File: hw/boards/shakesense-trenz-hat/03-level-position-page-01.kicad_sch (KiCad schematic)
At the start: 11 parts, among them J2 Passive GNSS antenna, U20 SCL3300-D01, U21 MAX-M10S

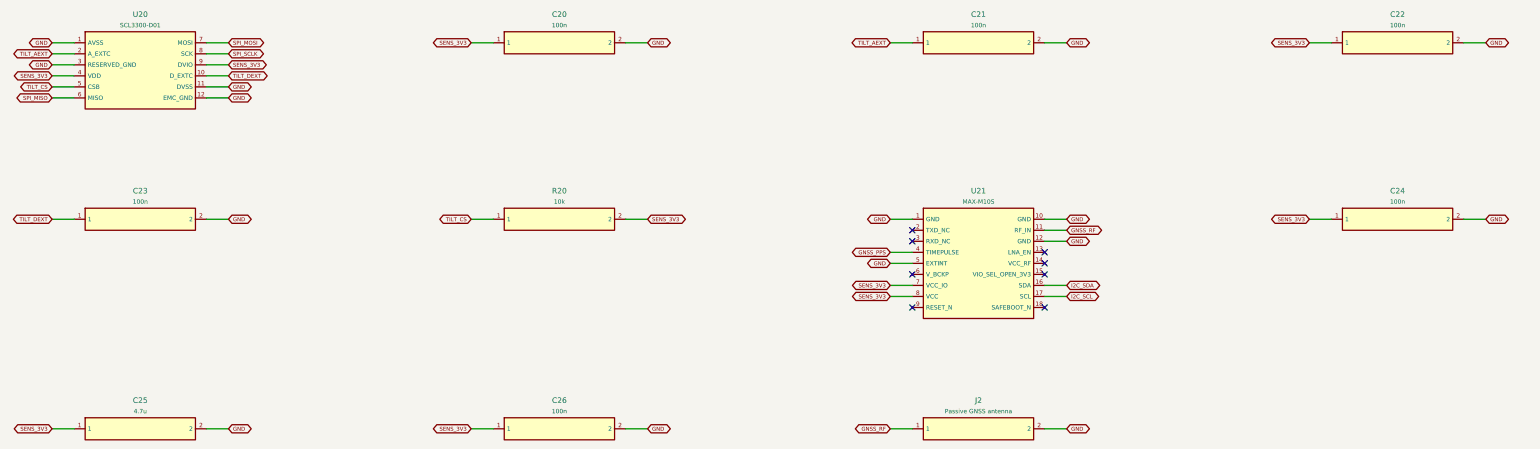
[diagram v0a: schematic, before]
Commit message: Expose Trenz GPIOs on the Pi-outline HDI sensor HAT
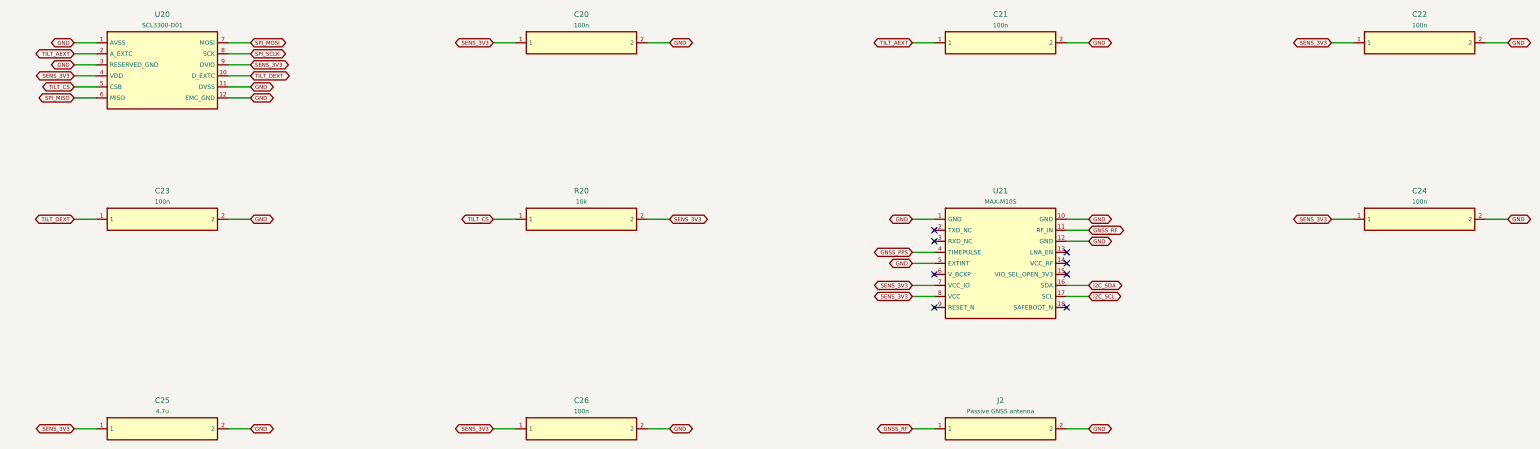
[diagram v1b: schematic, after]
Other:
- title: shakesense-trenz-hat / 03-level-position-page-01 -> ShakeSense T1 / 03-level-position-page-01
- moved on the sheet: C20, C21, C22, C23, C24, C25, C26, J2, R20, U20, U21

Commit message: Replace T1 GNSS with single Racotech geophone input
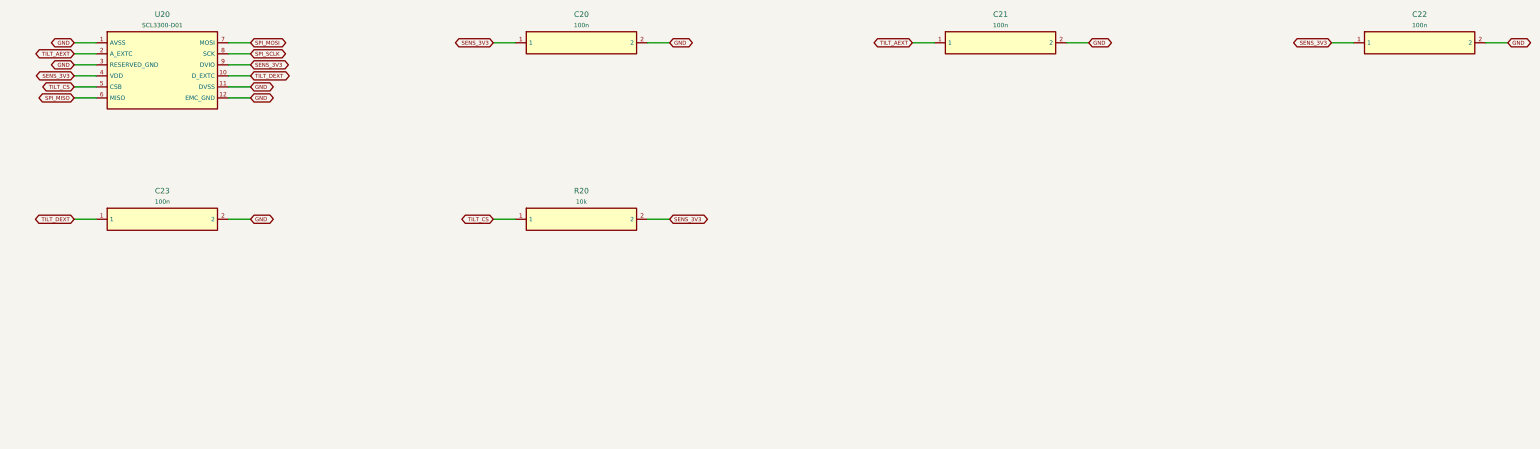
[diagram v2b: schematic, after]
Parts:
- removed C24: 100n, ShakeSense:Capacitor_SMD__C_0603_1608Metric, symbol ShakeSense:Part_C24
- removed C25: 4.7u, ShakeSense:Capacitor_SMD__C_0805_2012Metric, symbol ShakeSense:Part_C25
- removed C26: 100n, ShakeSense:Capacitor_SMD__C_0603_1608Metric, symbol ShakeSense:Part_C26
- removed J2: Passive GNSS antenna, ShakeSense:Connector_Coaxial__U.FL_Hirose_U.FL-R-SMT-1_Vertical, symbol ShakeSense:Part_J2
- removed U21: MAX-M10S, ShakeSense:RF_GPS__ublox_MAX, symbol ShakeSense:Part_U21
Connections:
- no-connect marks 8 -> 0
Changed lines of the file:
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@@
-(kicad_sch (version 20230121) (generator eeschema) (paper "A3") (title_block (title "ShakeSense T1 / 03-level-position-page-01") (date "2026-09-24") (rev "T1-GPIO"))
+(kicad_sch (version 20230121) (generator eeschema) (paper "A3") (title_block (title "ShakeSense T1 / 03-level-position-page-01") (date "2026-09-24") (rev "T1-GEO"))
 (symbol (lib_id "ShakeSense:Part_U20") (at 50.8 44.45 0) (unit 1) (in_bom yes) (on_board yes) (dnp no)
               (property "Reference" "U20" (at 50.8 31.560000000000002 0) (effects (font (size 1.27 1.27))))
@@
 (wire (pts (xy 162.56 78.74) (xy 167.64 78.74)) (stroke (width 0) (type default)))
 (global_label "SENS_3V3" (shape bidirectional) (at 167.64 78.74 0) (effects (font (size 0.9 0.9)) (justify left)))
-(symbol (lib_id "ShakeSense:Part_U21") (at 243.83999999999997 88.9 0) (unit 1) (in_bom yes) (on_board yes) (dnp no)
-              (property "Reference" "U21" (at 243.83999999999997 72.2 0) (effects (font (size 1.27 1.27))))
-              (property "Value" "MAX-M10S" (at 243.83999999999997 74.7 0) (effects (font (size 1.0 1.0))))
-              (property "Footprint" "ShakeSense:RF_GPS__ublox_MAX" (at 243.83999999999997 88.9 0) (effects (font (size 1 1)) hide))
-              (property "MPN" "MAX-M10S-00B" (at 243.83999999999997 88.9 0) (effects (font (size 1 1)) hide))
-              (instances (project "shakesense-trenz-hat" (path "/4ffaaa5d-c728-540d-9f0f-f1cafbdbe36e/30b3f632-5bdc-5bfd-9387-e670932c7991" (reference "U21") (unit 1)))))
-(wire (pts (xy 228.6 78.74) (xy 223.52 78.74)) (stroke (width 0) (type default)))
-(global_label "GND" (shape bidirectional) (at 223.52 78.74 180) (effects (font (size 0.9 0.9)) (justify right)))
-(no_connect (at 228.6 81.28))
-(no_connect (at 228.6 83.82))
-(wire (pts (xy 228.6 86.36) (xy 223.52 86.36)) (stroke (width 0) (type default)))
-(global_label "GNSS_PPS" (shape bidirectional) (at 223.52 86.36 180) (effects (font (size 0.9 0.9)) (justify right)))
-(wire (pts (xy 228.6 88.9) (xy 223.52 88.9)) (stroke (width 0) (type default)))
-(global_label "GND" (shape bidirectional) (at 223.52 88.9 180) (effects (font (size 0.9 0.9)) (justify right)))
-(no_connect (at 228.6 91.44))
-(wire (pts (xy 228.6 93.98) (xy 223.52 93.98)) (stroke (width 0) (type default)))
-(global_label "SENS_3V3" (shape bidirectional) (at 223.52 93.98 180) (effects (font (size 0.9 0.9)) (justify right)))
-(wire (pts (xy 228.6 96.52) (xy 223.52 96.52)) (stroke (width 0) (type default)))
-(global_label "SENS_3V3" (shape bidirectional) (at 223.52 96.52 180) (effects (font (size 0.9 0.9)) (justify right)))
-(no_connect (at 228.6 99.06))
-(wire (pts (xy 259.08 78.74) (xy 264.16 78.74)) (stroke (width 0) (type default)))
-(global_label "GND" (shape bidirectional) (at 264.16 78.74 0) (effects (font (size 0.9 0.9)) (justify left)))
-(wire (pts (xy 259.08 81.28) (xy 264.16 81.28)) (stroke (width 0) (type default)))
-(global_label "GNSS_RF" (shape bidirectional) (at 264.16 81.28 0) (effects (font (size 0.9 0.9)) (justify left)))
-(wire (pts (xy 259.08 83.82) (xy 264.16 83.82)) (stroke (width 0) (type default)))
-(global_label "GND" (shape bidirectional) (at 264.16 83.82 0) (effects (font (size 0.9 0.9)) (justify left)))
-(no_connect (at 259.08 86.36))
-(no_connect (at 259.08 88.9))
-(no_connect (at 259.08 91.44))
-(wire (pts (xy 259.08 93.98) (xy 264.16 93.98)) (stroke (width 0) (type default)))
-(global_label "I2C_SDA" (shape bidirectional) (at 264.16 93.98 0) (effects (font (size 0.9 0.9)) (justify left)))
-(wire (pts (xy 259.08 96.52) (xy 264.16 96.52)) (stroke (width 0) (type default)))
-(global_label "I2C_SCL" (shape bidirectional) (at 264.16 96.52 0) (effects (font (size 0.9 0.9)) (justify left)))
-(no_connect (at 259.08 99.06))
-(symbol (lib_id "ShakeSense:Part_C24") (at 340.35999999999996 78.74000000000001 0) (unit 1) (in_bom yes) (on_board yes) (dnp no)
-              (property "Reference" "C24" (at 340.35999999999996 72.2 0) (effects (font (size 1.27 1.27))))
-              (property "Value" "100n" (at 340.35999999999996 74.7 0) (effects (font (size 1.0 1.0))))
-              (property "Footprint" "ShakeSense:Capacitor_SMD__C_0603_1608Metric" (at 340.35999999999996 78.74000000000001 0) (effects (font (size 1 1)) hide))
-              (property "MPN" "GRM188R71H104KA93D" (at 340.35999999999996 78.74000000000001 0) (effects (font (size 1 1)) hide))
-              (instances (project "shakesense-trenz-hat" (path "/4ffaaa5d-c728-540d-9f0f-f1cafbdbe36e/30b3f632-5bdc-5bfd-9387-e670932c7991" (reference "C24") (unit 1)))))
-(wire (pts (xy 325.12 78.74) (xy 320.04 78.74)) (stroke (width 0) (type default)))
-(global_label "SENS_3V3" (shape bidirectional) (at 320.04 78.74 180) (effects (font (size 0.9 0.9)) (justify right)))
-(wire (pts (xy 355.6 78.74) (xy 360.68 78.74)) (stroke (width 0) (type default)))
-(global_label "GND" (shape bidirectional) (at 360.68 78.74 0) (effects (font (size 0.9 0.9)) (justify left)))
-(symbol (lib_id "ShakeSense:Part_C25") (at 50.8 127.00000000000001 0) (unit 1) (in_bom yes) (on_board yes) (dnp no)
-              (property "Reference" "C25" (at 50.8 120.46000000000001 0) (effects (font (size 1.27 1.27))))
-              (property "Value" "4.7u" (at 50.8 122.96000000000001 0) (effects (font (size 1.0 1.0))))
-              (property "Footprint" "ShakeSense:Capacitor_SMD__C_0805_2012Metric" (at 50.8 127.00000000000001 0) (effects (font (size 1 1)) hide))
-              (property "MPN" "GRM21BR71A475KA73L" (at 50.8 127.00000000000001 0) (effects (font (size 1 1)) hide))
-              (instances (project "shakesense-trenz-hat" (path "/4ffaaa5d-c728-540d-9f0f-f1cafbdbe36e/30b3f632-5bdc-5bfd-9387-e670932c7991" (reference "C25") (unit 1)))))
-(wire (pts (xy 35.56 127.0) (xy 30.48 127.0)) (stroke (width 0) (type default)))
-(global_label "SENS_3V3" (shape bidirectional) (at 30.48 127.0 180) (effects (font (size 0.9 0.9)) (justify right)))
-(wire (pts (xy 66.04 127.0) (xy 71.12 127.0)) (stroke (width 0) (type default)))
-(global_label "GND" (shape bidirectional) (at 71.12 127.0 0) (effects (font (size 0.9 0.9)) (justify left)))
-(symbol (lib_id "ShakeSense:Part_C26") (at 147.32 127.00000000000001 0) (unit 1) (in_bom yes) (on_board yes) (dnp no)
-              (property "Reference" "C26" (at 147.32 120.46000000000001 0) (effects (font (size 1.27 1.27))))
-              (property "Value" "100n" (at 147.32 122.96000000000001 0) (effects (font (size 1.0 1.0))))
-              (property "Footprint" "ShakeSense:Capacitor_SMD__C_0603_1608Metric" (at 147.32 127.00000000000001 0) (effects (font (size 1 1)) hide))
-              (property "MPN" "GRM188R71H104KA93D" (at 147.32 127.00000000000001 0) (effects (font (size 1 1)) hide))
-              (instances (project "shakesense-trenz-hat" (path "/4ffaaa5d-c728-540d-9f0f-f1cafbdbe36e/30b3f632-5bdc-5bfd-9387-e670932c7991" (reference "C26") (unit 1)))))
-(wire (pts (xy 132.08 127.0) (xy 127.0 127.0)) (stroke (width 0) (type default)))
-(global_label "SENS_3V3" (shape bidirectional) (at 127.0 127.0 180) (effects (font (size 0.9 0.9)) (justify right)))
-(wire (pts (xy 162.56 127.0) (xy 167.64 127.0)) (stroke (width 0) (type default)))
-(global_label "GND" (shape bidirectional) (at 167.64 127.0 0) (effects (font (size 0.9 0.9)) (justify left)))
-(symbol (lib_id "ShakeSense:Part_J2") (at 243.83999999999997 127.00000000000001 0) (unit 1) (in_bom yes) (on_board yes) (dnp no)
-              (property "Reference" "J2" (at 243.83999999999997 120.46000000000001 0) (effects (font (size 1.27 1.27))))
-              (property "Value" "Passive GNSS antenna" (at 243.83999999999997 122.96000000000001 0) (effects (font (size 1.0 1.0))))
-              (property "Footprint" "ShakeSense:Connector_Coaxial__U.FL_Hirose_U.FL-R-SMT-1_Vertical" (at 243.83999999999997 127.00000000000001 0) (effects (font (size 1 1)) hide))
-              (property "MPN" "U.FL-R-SMT-1(10)" (at 243.83999999999997 127.00000000000001 0) (effects (font (size 1 1)) hide))
-              (instances (project "shakesense-trenz-hat" (path "/4ffaaa5d-c728-540d-9f0f-f1cafbdbe36e/30b3f632-5bdc-5bfd-9387-e670932c7991" (reference "J2") (unit 1)))))
-(wire (pts (xy 228.6 127.0) (xy 223.52 127.0)) (stroke (width 0) (type default)))
-(global_label "GNSS_RF" (shape bidirectional) (at 223.52 127.0 180) (effects (font (size 0.9 0.9)) (justify right)))
-(wire (pts (xy 259.08 127.0) (xy 264.16 127.0)) (stroke (width 0) (type default)))
-(global_label "GND" (shape bidirectional) (at 264.16 127.0 0) (effects (font (size 0.9 0.9)) (justify left)))
 )
